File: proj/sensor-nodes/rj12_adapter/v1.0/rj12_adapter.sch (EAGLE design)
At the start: 54 parts, among them J1 54602-908LF, J2 54602-908LF, U2 PCA9615DPJ, U3 MIC4680YM-TR, U4 LM2937IMP3.3NOPB, U5 APDS-9250, U7 TSL2591

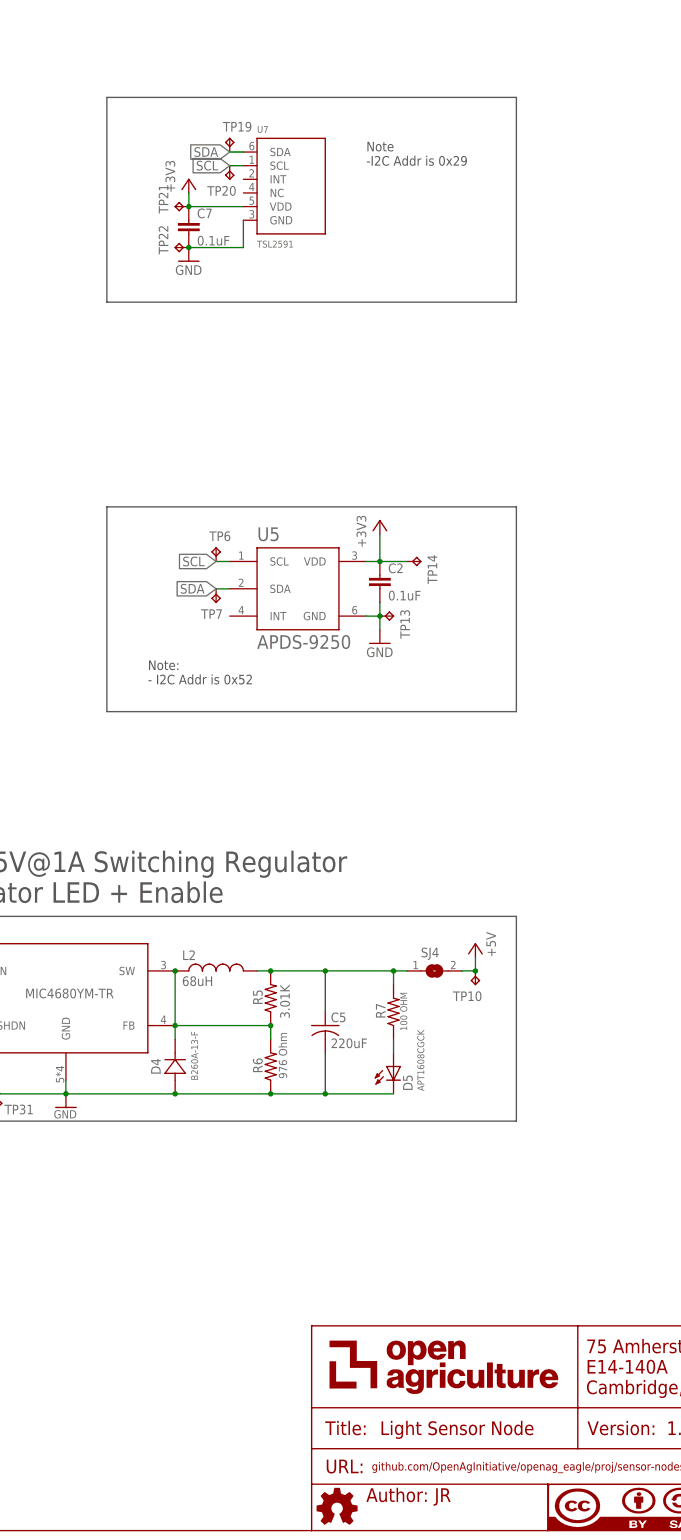
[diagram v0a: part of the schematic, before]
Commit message: extracted design blocks from light controller
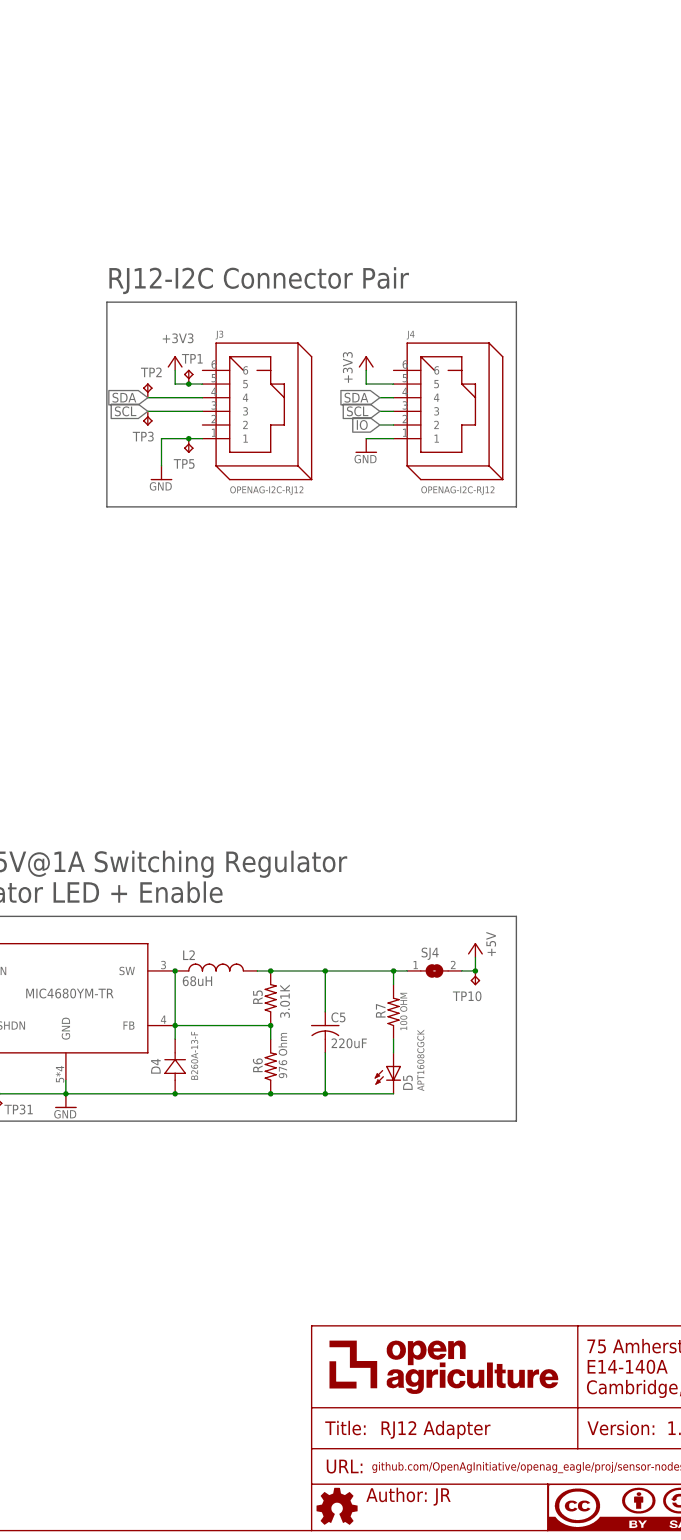
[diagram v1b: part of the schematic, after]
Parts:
- removed C2, C7: 0.1uF, openag-capacitors:0.1UF-C0603C104K5RACTU
- removed TP13, TP14, TP19, TP20, TP21, TP22, TP6, TP7: TPTP06R, openag-testpads:TPTP06R
- removed U5: APDS-9250, openag-sensors:APDS-9250
- removed U7: TSL2591, openag-sensors:TSL25911FN
- added J3, J4: OPENAG-I2C-RJ12, openag-connectors:OPENAG-I2C-RJ12
- added TP1, TP2, TP3, TP5: TPTP06R, openag-testpads:TPTP06R
- FRAME1: TITLE Light Sensor Node -> RJ12 Adapter
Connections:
- new net IO: J4.2
- net +3V3: now also J3.5, J4.5, TP1.TP; no longer C2.1, C7.1, TP14.TP, TP21.TP, U5.VDD, U7.VDD
- net GND: now also J3.1, J4.1, TP5.TP; no longer C2.2, C7.2, TP13.TP, TP22.TP, U5.GND, U7.GND
- net SCL: now also J3.3, J4.3, TP3.TP; no longer TP20.TP, TP6.TP, U5.SCL, U7.SCL
- net SDA: now also J3.4, J4.4, TP2.TP; no longer TP19.TP, TP7.TP, U5.SDA, U7.SDA
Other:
- note added: "RJ12-I2C Connector Pair"
- note removed: "APDS-9250 Light Sensor"
- note removed: "Note -I2C Addr is 0x29"
- note removed: "Note: - I2C Addr is 0x52"
- note removed: "TSL2591 Light Intensity Sensor"

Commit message: added light and rj12 nodes, started working on light controller v2
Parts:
- removed J3, J4: OPENAG-I2C-RJ12, openag-connectors:OPENAG-I2C-RJ12
- removed L2: 68uH, openag-inductors:68UH-UP2B-680-R
- removed SJ4: (no value), openag-connectors:SOLDERJUMPERREFLOW_NOPASTE
- removed TP1, TP10, TP2, TP3, TP31: TPTP06R, openag-testpads:TPTP06R
- added J5, J6: OPENAG-I2C-RJ12, openag-connectors:OPENAG-I2C-RJ12
- added L1: 68uH, openag-inductors:68UH-UP2B-680-R
- added SJ2: (no value), openag-connectors:SOLDERJUMPERREFLOW_NOPASTE
- added TP13, TP14, TP6, TP7: TPTP06R, openag-testpads:TPTP06R
- C4: device openag-capacitors:15UF-TPSD156K035R0100 -> openag-capacitors:15UF-C2012X5R1V156M125AC
- D4: value B260A-13-F -> SBR2A40P1-7; device openag-diodes:B260A-13-F -> openag-diodes:SBR2A40P1-7
- R13, R15, R16, R17: value NV -> 600; device openag-resistors:R0603 -> openag-resistors:600OHM-RC0603FR-07604RL
- R14, R19: value NV -> 120; device openag-resistors:R0603 -> openag-resistors:120OHM-RC0603FR-07120RL
- R2, R7: value 100 OHM -> 100
- R20, R21: value NV -> 10K; device openag-resistors:R0603 -> openag-resistors:10K-ERJ-3EKF1002V
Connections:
- net +24V: now also C4.1, TP7.TP; no longer C4.1(+), TP12.TP
- net +3V3: now also J5.5, J6.5, TP11.TP; no longer J3.5, J4.5, TP1.TP
- net +5V: now also SJ2.2, TP5.TP; no longer SJ4.2, TP10.TP
- net GND: now also C4.2, J5.1, J6.1, TP13.TP, TP6.TP, U4.TAB; no longer C4.2(-), J3.1, J4.1, TP11.TP, TP31.TP, TP5.TP
- net IO: now also J6.2; no longer J4.2
- net N$31: now also L1.1; no longer L2.1
- net N$33: now also L1.2, SJ2.1; no longer L2.2, SJ4.1
- net SCL: now also J5.3, J6.3, TP12.TP; no longer J3.3, J4.3, TP3.TP
- net SDA: now also J5.4, J6.4, TP14.TP; no longer J3.4, J4.4, TP2.TP
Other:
- note added: "3.3V@400mA Regulator"
- note removed: "3.3V, 400mA Regulator"
- moved on the sheet: C4, C5, D5, R5, R6, R7, TP11, TP12, TP5, U3
